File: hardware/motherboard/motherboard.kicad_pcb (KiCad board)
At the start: 2 copper layers, 65 x 56 mm, 5 parts, among them P1 Conn_02x20_Odd_Even

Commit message: imported pcb
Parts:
- moved MK4 235.5 mm to (51.5, 253.1), turned to 270 degrees
- moved MK2 223.9 mm to (100.5, 253.1), turned to 90 degrees
- moved MK3 159.6 mm to (51.5, 195.1), turned to 270 degrees
- moved P1 148.8 mm to (99.2, 200.0), turned to 180 degrees
- moved MK1 141.9 mm to (100.5, 195.1), turned to 90 degrees
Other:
- board size 65 x 56 mm -> 237 x 156.6 mm

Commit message: work on hardware motherboard
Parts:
- removed MK1, MK2, MK3, MK4: M2.5, MountingHole:MountingHole_2.7mm_M2.5
- added C1: 10µF, Capacitor_THT:CP_Radial_D6.3mm_P2.50mm, F.Cu at (266.2, 119.4)
- added C10: 1000µF, Capacitor_THT:CP_Radial_D10.0mm_P5.00mm, F.Cu at (275.8, 123.7)
- added C11: 100nF, Capacitor_THT:C_Disc_D5.0mm_W2.5mm_P5.00mm, F.Cu at (262.8, 170.7)
- added C12: 1000µF, Capacitor_THT:CP_Radial_D10.0mm_P5.00mm, F.Cu at (275.9, 156.5)
- added C13: 1000µF, Capacitor_THT:CP_Radial_D10.0mm_P5.00mm, F.Cu at (275.9, 146.7)
- added C14: 1000µF, Capacitor_THT:CP_Radial_D10.0mm_P5.00mm, F.Cu at (275.7, 184.8)
- added C15: 100nF, Capacitor_THT:C_Disc_D5.0mm_W2.5mm_P5.00mm, F.Cu at (259.7, 127.0)
- added C16: 100nF, Capacitor_THT:C_Disc_D5.0mm_W2.5mm_P5.00mm, F.Cu at (259.2, 165.7)
- added C2: 10µF, Capacitor_THT:CP_Radial_D6.3mm_P2.50mm, F.Cu at (264.3, 157.8)
- added C3: 10µF, Capacitor_THT:CP_Radial_D6.3mm_P2.50mm, F.Cu at (258.1, 119.5)
- added C4: 10µF, Capacitor_THT:CP_Radial_D6.3mm_P2.50mm, F.Cu at (256.1, 157.8)
- added C5: 8n2, Capacitor_THT:C_Disc_D5.0mm_W2.5mm_P5.00mm, F.Cu at (255.8, 131.9)
- added C6: 470µF, Capacitor_THT:CP_Radial_D10.0mm_P5.00mm, F.Cu at (275.9, 135.3)
- added C7: 8n2, Capacitor_THT:C_Disc_D5.0mm_W2.5mm_P5.00mm, F.Cu at (255.2, 170.6)
- added C8: 470µF, Capacitor_THT:CP_Radial_D10.0mm_P5.00mm, F.Cu at (276.1, 167.9)
- added C9: 100nF, Capacitor_THT:C_Disc_D5.0mm_W2.5mm_P5.00mm, F.Cu at (263.4, 131.9)
- added J1: Conn_01x04_Female, Connector_PinSocket_2.54mm:PinSocket_1x04_P2.54mm_Vertical, F.Cu at (161.0, 107.0)
- added J1: Conn_01x04_Female, Connector_PinSocket_2.54mm:PinSocket_1x04_P2.54mm_Vertical, F.Cu at (158.5, 139.3)
- added J10: Conn_01x02_Female, TerminalBlock:TerminalBlock_bornier-2_P5.08mm, F.Cu at (267.0, 194.0)
- added J11: Conn_01x02_Female, TerminalBlock:TerminalBlock_bornier-2_P5.08mm, F.Cu at (255.0, 194.0)
- added J2: AudioJack3_Ground, Connector_Audio:Jack_3.5mm_CUI_SJ-3523-SMT_Horizontal, F.Cu at (270.8, 107.2)
- added J3: Conn_01x05_Female, TerminalBlock:TerminalBlock_bornier-5_P5.08mm, F.Cu at (175.0, 194.4)
- added J4: Conn_01x05_Female, Connector_TE-Connectivity:TE_826576-5_1x05_P3.96mm_Vertical, F.Cu at (195.0, 175.0)
- added J5: Conn_01x05_Female, Connector_PinSocket_2.54mm:PinSocket_1x05_P2.54mm_Vertical, F.Cu at (185.6, 117.0)
- added J6: Conn_01x05_Female, Connector_PinSocket_2.54mm:PinSocket_1x05_P2.54mm_Vertical, F.Cu at (218.0, 117.0)
- added J7: Conn_01x05_Female, Connector_PinSocket_2.54mm:PinSocket_1x05_P2.54mm_Vertical, F.Cu at (219.0, 194.4)
- added J8: Conn_01x02_Female, TerminalBlock:TerminalBlock_bornier-2_P5.08mm, F.Cu at (146.0, 194.4)
- added J9: Conn_01x03_Female, TerminalBlock:TerminalBlock_bornier-3_P5.08mm, F.Cu at (202.0, 194.4)
- added K2: SANYOU_SRD_Form_C, Relay_THT:Relay_SPDT_SANYOU_SRD_Series_Form_C, F.Cu at (174.0, 168.0)
- added Q1: BSS138, Package_TO_SOT_SMD:SOT-23, F.Cu at (171.0, 150.0)
- added Q2: BSS138, Package_TO_SOT_SMD:SOT-23, F.Cu at (160.0, 150.0)
- added Q3: BSS138, Package_TO_SOT_SMD:SOT-23, F.Cu at (147.0, 184.0)
- added R1: 10K, Resistor_THT:R_Axial_DIN0207_L6.3mm_D2.5mm_P7.62mm_Horizontal, F.Cu at (174.6, 154.0)
- added R10: 4R7, Resistor_THT:R_Axial_DIN0207_L6.3mm_D2.5mm_P7.62mm_Horizontal, F.Cu at (263.4, 135.9)
- added R11: 470R, Resistor_THT:R_Axial_DIN0207_L6.3mm_D2.5mm_P7.62mm_Horizontal, F.Cu at (262.9, 184.9)
- added R12: 4R7, Resistor_THT:R_Axial_DIN0207_L6.3mm_D2.5mm_P7.62mm_Horizontal, F.Cu at (262.9, 173.9)
- added R13: 1R, Resistor_THT:R_Axial_DIN0207_L6.3mm_D2.5mm_P7.62mm_Horizontal, F.Cu at (259.7, 143.6)
- added R14: 1R, Resistor_THT:R_Axial_DIN0207_L6.3mm_D2.5mm_P7.62mm_Horizontal, F.Cu at (259.2, 173.9)
- added R15: 10K, Resistor_THT:R_Axial_DIN0207_L6.3mm_D2.5mm_P7.62mm_Horizontal, F.Cu at (167.0, 179.0)
- added R2: 10K, Resistor_THT:R_Axial_DIN0207_L6.3mm_D2.5mm_P7.62mm_Horizontal, F.Cu at (164.0, 154.0)
- added R3: 10K, Resistor_THT:R_Axial_DIN0207_L6.3mm_D2.5mm_P7.62mm_Horizontal, F.Cu at (143.0, 188.0)
- added R4: 10K, Resistor_THT:R_Axial_DIN0207_L6.3mm_D2.5mm_P7.62mm_Horizontal, F.Cu at (167.0, 157.0)
- added R5: 10K, Resistor_THT:R_Axial_DIN0207_L6.3mm_D2.5mm_P7.62mm_Horizontal, F.Cu at (156.4, 157.0)
- added R6: 10K, Resistor_THT:R_Axial_DIN0207_L6.3mm_D2.5mm_P7.62mm_Horizontal, F.Cu at (140.0, 188.0)
- added R7: 100R, Resistor_THT:R_Axial_DIN0207_L6.3mm_D2.5mm_P7.62mm_Horizontal, F.Cu at (255.8, 143.6)
- added R8: 100R, Resistor_THT:R_Axial_DIN0207_L6.3mm_D2.5mm_P7.62mm_Horizontal, F.Cu at (255.2, 181.6)
- added R9: 470R, Resistor_THT:R_Axial_DIN0207_L6.3mm_D2.5mm_P7.62mm_Horizontal, F.Cu at (263.4, 147.6)
- added RV1: 10K, Potentiometer_SMD:Potentiometer_Bourns_3314J_Vertical, F.Cu at (248.3, 119.4)
- added RV2: 10K, Potentiometer_SMD:Potentiometer_Bourns_3314J_Vertical, F.Cu at (248.9, 157.7)
- added U1: TDA2003, Package_TO_SOT_THT:TO-220-5_P3.4x3.7mm_StaggerOdd_Lead3.8mm_Vertical, F.Cu at (246.0, 175.4)
- added U2: TDA2003, Package_TO_SOT_THT:TO-220-5_P3.4x3.7mm_StaggerOdd_Lead3.8mm_Vertical, F.Cu at (246.0, 139.7)
- moved P1 100.4 mm to (56.9, 109.0)
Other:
- board size 237 x 156.6 mm -> 279.3 x 100 mm

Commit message: layout of first mb; test print
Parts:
- removed the J1 at (161.0, 107.0)
- removed the J1 at (158.5, 139.3)
- removed R2, R5: 10K, Resistor_THT:R_Axial_DIN0207_L6.3mm_D2.5mm_P7.62mm_Horizontal
- added C17: 1000µF, Capacitor_THT:CP_Radial_D10.0mm_P5.00mm, F.Cu at (152.5, 127.8)
- added D1: 1N4148W, Diode_SMD:D_SOD-123, F.Cu at (204.8, 184.5)
- added J1: Conn_01x04_Female, Connector_PinSocket_2.54mm:PinSocket_1x04_P2.54mm_Vertical, F.Cu at (139.0, 111.2)
- added J1: Conn_01x04_Female, Connector_PinSocket_2.54mm:PinSocket_1x04_P2.54mm_Vertical, F.Cu at (105.0, 108.7)
- added M1: Fan_3pin, Connector:FanPinHeader_1x03_P2.54mm_Vertical, F.Cu at (103.0, 157.5)
- added M2: Fan_3pin, Connector:FanPinHeader_1x03_P2.54mm_Vertical, F.Cu at (103.0, 148.5)
- J2: value AudioJack3_Ground -> Conn_01x03_Male; footprint Connector_Audio:Jack_3.5mm_CUI_SJ-3523-SMT_Horizontal -> Connector_PinHeader_2.54mm:PinHeader_1x03_P2.54mm_Vertical
- J5: value Conn_01x05_Female -> Conn_01x06_Female; footprint Connector_PinSocket_2.54mm:PinSocket_1x05_P2.54mm_Vertical -> Connector_PinSocket_2.54mm:PinSocket_1x06_P2.54mm_Vertical
- P1: moved to F.Cu
- moved J2 116.7 mm to (154.2, 113.2), turned to 270 degrees
- moved C2 115.7 mm to (159.2, 109.2), turned to 90 degrees
- moved RV2 110.8 mm to (150.2, 107.2), turned to 270 degrees
- moved C1 107.0 mm to (159.2, 117.2), turned to 270 degrees
- moved C4 101.2 mm to (167.2, 109.2), turned to 90 degrees
- moved RV1 98.1 mm to (150.2, 119.2), turned to 270 degrees
- moved C13 97.9 mm to (180.5, 168.5), turned to 0 degrees
- moved C6 97.8 mm to (180.5, 156.8), turned to 0 degrees
- moved C10 97.8 mm to (180.5, 145.5), turned to 0 degrees
- moved J10 91.3 mm to (175.8, 196.0)
- moved U1 91.2 mm to (179.5, 113.0), turned to 0 degrees
- moved C3 90.9 mm to (167.2, 117.2), turned to 270 degrees
- moved C14 79.6 mm to (197.8, 168.5), turned to 0 degrees
- moved R4 79.4 mm to (231.0, 110.0), turned to 180 degrees
- moved C8 79.1 mm to (197.8, 157.0), turned to 0 degrees
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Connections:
- net /MOTOR_SIGNAL renamed Net-(J5-Pad4)
- J3 pad 3: +3V3 -> +12V
- J3 pad 5: +12V -> +3V3
- J5 pad 3: /MOTOR_ZF -> +5V
- J5 pad 5: +5V -> Net-(J5-Pad5)
- J7 pad 2: /M3_HA -> /M1_HA
- J7 pad 4: /M1_HA -> /M3_HA
- K2 pad 2: GND -> Net-(D1-Pad2)
- K2 pad 4: Net-(K2-Pad4) -> GND
- K2 pad 5: /MOTOR_RELAY -> +5V
- P1 pad 1: +3V3 -> Net-(P1-Pad1)
- P1 pad 17: +3V3 -> Net-(P1-Pad1)
- Q2 pad 1: +3V3 -> /GPIO13(PWM1)
- Q2 pad 2: /GPIO13(PWM1) -> GND
- Q2 pad 3: /MOTOR_RELAY -> Net-(D1-Pad2)
- R15 pad 2: /MOTOR_RELAY -> /GPIO13(PWM1)
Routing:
- net +5V: track 0.00 -> 433.2 mm
- net +3V3: track 0.00 -> 232.2 mm
- net /GPIO12(PWM0): track 0.00 -> 199.0 mm, vias 0 -> 1
- net +12V: track 0.00 -> 186.4 mm
- net /GPIO13(PWM1): track 0.00 -> 104.2 mm
- net /GPIO11(SPI0_SCK): track 0.00 -> 98.5 mm
- net /AMP2_LS: track 0.00 -> 93.7 mm
- net /AMP1_LS: track 0.00 -> 90.6 mm
- net /M3_HA: track 0.00 -> 88.4 mm
- net /M2_HA: track 0.00 -> 86.9 mm
- net /M1_HA: track 0.00 -> 85.3 mm
- net /GPIO3(SCL1): track 0.00 -> 73.9 mm
- net /GPIO2(SDA1): track 0.00 -> 73.9 mm
- net Net-(C13-Pad1): track 0.00 -> 71.4 mm
- net Net-(C14-Pad1): track 0.00 -> 71.2 mm
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- added copper zone on B.Cu, net GND
- added copper zone on F.Cu, net GND
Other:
- board size 279.3 x 100 mm -> 160 x 100 mm
- board text removed: "CAMERA"
- board text removed: "DISPLAY"
- board text removed: "RASPBERRY-PI 40-PIN ADDON BOARD VIEW FROM TOP NOTE: P1 SHOULD BE FITTED ON THE REVERSE OF THE BOARD ADD EDGE CUTS FROM CAMERA AND DISPLAY PORTS AS REQUIRED"
- board text removed: "RJ45"
- board text removed: "USB"

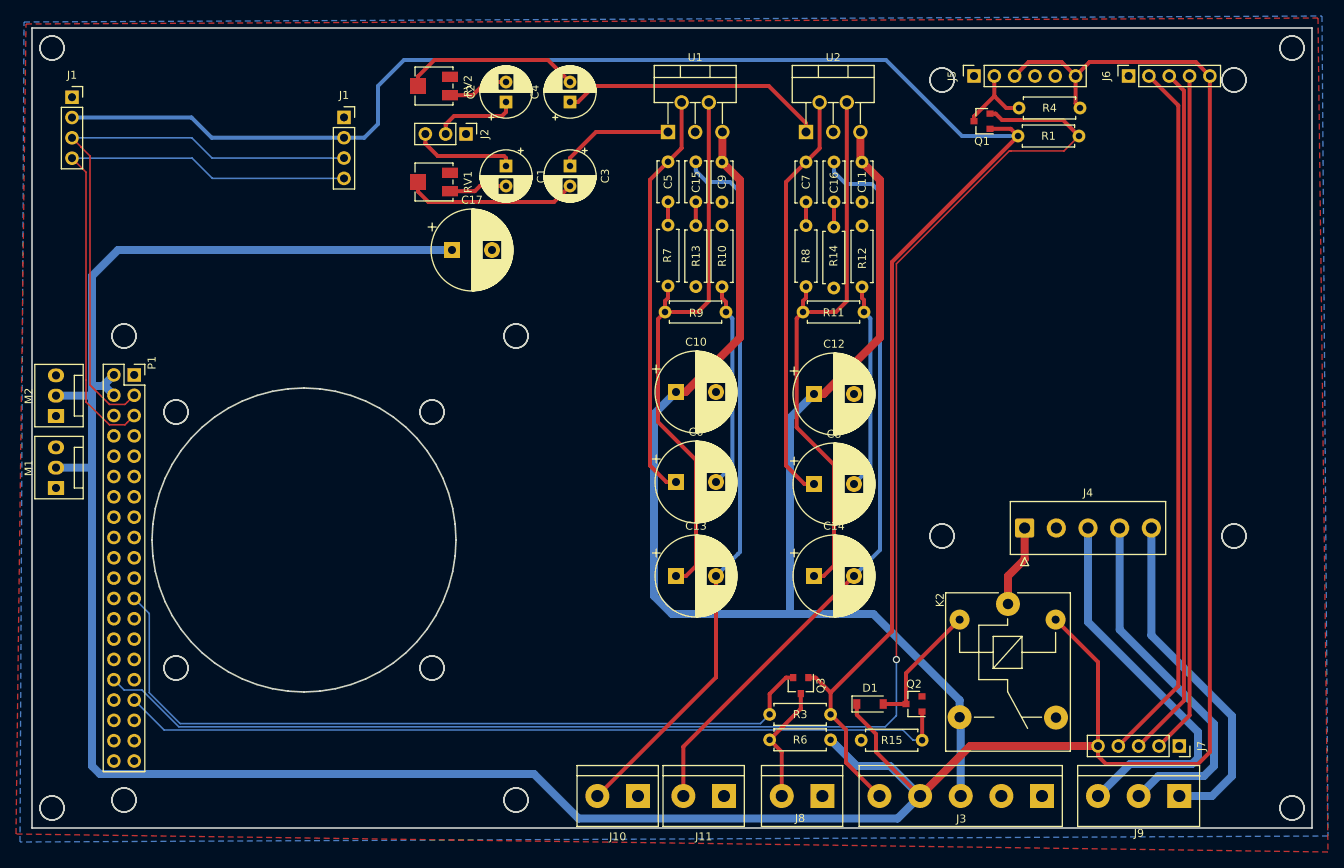
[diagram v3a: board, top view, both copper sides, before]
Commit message: ordered first version
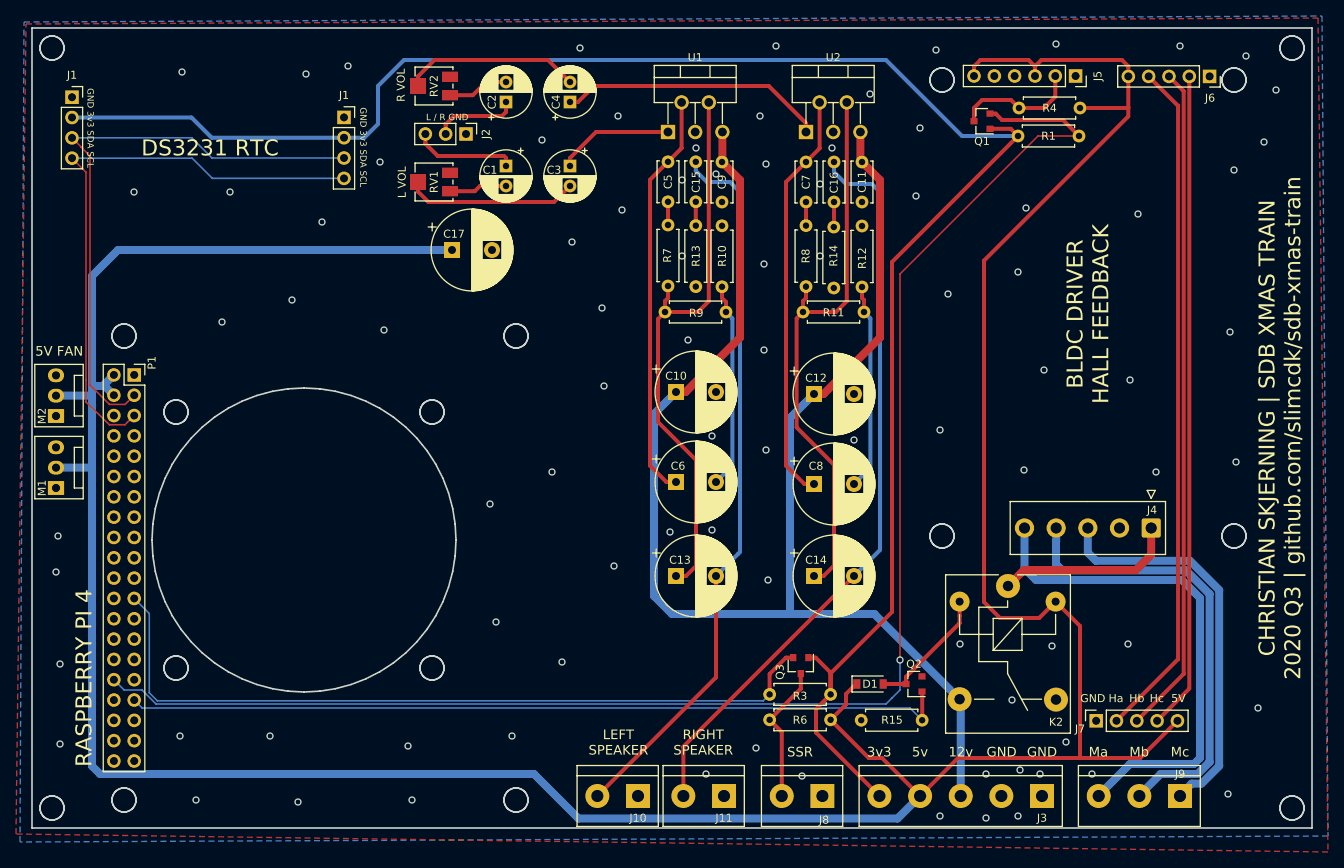
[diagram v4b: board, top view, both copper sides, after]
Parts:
- moved J4 15.8 mm to (239.9, 162.5), turned to 180 degrees
- moved J5 12.7 mm to (230.4, 106.0), turned to 270 degrees
- moved J7 10.9 mm to (233.0, 186.6), turned to 90 degrees
- moved J6 10.1 mm to (247.2, 106.0), turned to 270 degrees
- moved D1 2.50 mm to (204.8, 182.0)
- moved Q2 2.50 mm to (210.2, 182.0)
- moved Q3 2.50 mm to (196.1, 179.7)
- moved R15 2.50 mm to (203.7, 186.5)
- moved R3 2.50 mm to (199.8, 183.3)
- moved R6 2.50 mm to (199.8, 186.5)
- moved K2 2.25 mm to (222.0, 169.8)
- moved J9 0.09 mm to (243.5, 196.0)
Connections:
- J9 pad 1: /M3 -> /M1
- J9 pad 3: /M1 -> /M3
- P1 pad 17: Net-(P1-Pad1) -> Net-(P1-Pad17)
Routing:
- net /M3: track 42.8 -> 63.2 mm
- net Net-(J4-Pad1): track 10.4 -> 22.9 mm
- net +5V: track 433.2 -> 421.2 mm
- net /M2: track 45.6 -> 56.9 mm
- net /M3_HA: track 88.4 -> 82.2 mm
- net /MOTOR_VR: track 10.4 -> 15.8 mm
- net /GPIO12(PWM0): track 199.0 -> 194.0 mm
- net +3V3: track 232.2 -> 236.4 mm
- net /M2_HA: track 86.9 -> 83.7 mm
- net /SSR_RELAY: track 15.0 -> 17.5 mm
- net /GPIO11(SPI0_SCK): track 98.5 -> 97.2 mm
- net /M1: track 48.9 -> 50.0 mm
- net /GPIO13(PWM1): track 104.2 -> 103.1 mm
- net (no net): vias 0 -> 90
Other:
- board text added: "12v"
- board text added: "3v3"
- board text added: "5V"
- board text added: "5V FAN"
- board text added: "5v"
- board text added: "BLDC DRIVER HALL FEEDBACK"
- board text added: "CHRISTIAN SKJERNING | SDB XMAS TRAIN 2020 Q3 | github.com/slimcdk/sdb-xmas-train"
- board text added: "DS3231 RTC"
- board text added: "GND"
- board text added: "GND 3v3 SDA SCL"
- board text added: "Ha"
- board text added: "Hb"
- board text added: "Hc"
- board text added: "L / R GND"
- board text added: "L VOL"
- board text added: "LEFT SPEAKER"
- board text added: "Ma"
- board text added: "Mb"
- board text added: "Mc"
- board text added: "R VOL"
- board text added: "RASPBERRY PI 4"
- board text added: "RIGHT SPEAKER"
- board text added: "SSR"

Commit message: pcb design v2
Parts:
- removed the J1 at (105.0, 108.7)
- removed M1, M2: Fan_3pin, Connector:FanPinHeader_1x03_P2.54mm_Vertical
- added C18: 1000µF, Capacitor_THT:CP_Radial_D5.0mm_P2.50mm, F.Cu at (28.5, 56.2)
- added D2: LED, LED_SMD:LED_1210_3225Metric_Pad1.42x2.65mm_HandSolder, F.Cu at (105.8, 122.8)
- added D3: LED, LED_SMD:LED_1210_3225Metric_Pad1.42x2.65mm_HandSolder, F.Cu at (105.8, 130.2)
- added D4: LED, LED_SMD:LED_1210_3225Metric_Pad1.42x2.65mm_HandSolder, F.Cu at (105.8, 137.8)
- added D5: LED, LED_SMD:LED_1210_3225Metric_Pad1.42x2.65mm_HandSolder, F.Cu at (28.5, 78.0)
- added D6: LED, LED_SMD:LED_1210_3225Metric_Pad1.42x2.65mm_HandSolder, F.Cu at (185.8, 73.6)
- added D7: LED, LED_SMD:LED_1210_3225Metric_Pad1.42x2.65mm_HandSolder, F.Cu at (173.6, 58.4)
- added D8: LED, LED_SMD:LED_1210_3225Metric_Pad1.42x2.65mm_HandSolder, F.Cu at (163.5, 38.5)
- added D9: LED, LED_SMD:LED_1210_3225Metric_Pad1.42x2.65mm_HandSolder, F.Cu at (104.5, 63.0)
- added J12: Conn_01x03_Male, Connector:FanPinHeader_1x03_P2.54mm_Vertical, F.Cu at (103.6, 147.7)
- added J13: Conn_01x03_Male, Connector:FanPinHeader_1x03_P2.54mm_Vertical, F.Cu at (113.3, 147.7)
- added J14: Conn_01x03_Male, Connector:FanPinHeader_1x03_P2.54mm_Vertical, F.Cu at (123.0, 147.7)
- added J15: Conn_01x06_Female, Connector_PinSocket_2.54mm:PinSocket_1x06_P2.54mm_Vertical, F.Cu at (58.0, 29.6)
- added R16: 10K, Resistor_SMD:R_1210_3225Metric_Pad1.42x2.65mm_HandSolder, B.Cu at (51.0, 106.8)
- added R17: ?, Resistor_SMD:R_1210_3225Metric_Pad1.42x2.65mm_HandSolder, F.Cu at (185.8, 79.0)
- added R18: ?, Resistor_SMD:R_1210_3225Metric_Pad1.42x2.65mm_HandSolder, F.Cu at (173.6, 64.3)
- added R19: 10K, Resistor_SMD:R_1210_3225Metric_Pad1.42x2.65mm_HandSolder, B.Cu at (47.0, 106.8)
- added R2: ?, Resistor_SMD:R_1210_3225Metric_Pad1.42x2.65mm_HandSolder, F.Cu at (105.8, 126.6)
- added R20: ?, Resistor_SMD:R_1210_3225Metric_Pad1.42x2.65mm_HandSolder, F.Cu at (167.5, 38.5)
- added R21: ?, Resistor_SMD:R_1210_3225Metric_Pad1.42x2.65mm_HandSolder, F.Cu at (104.4, 57.5)
- added R5: ?, Resistor_SMD:R_1210_3225Metric_Pad1.42x2.65mm_HandSolder, F.Cu at (28.5, 74.5)
- added REF**: Unknown_TO220_16x24mm_Heatsink, Local_Heatsink:Unknown_TO220_16x24mm_Heatsink, F.Cu at (172.2, 142.4)
- added REF**: Unknown_TO220_16x24mm_Heatsink, Local_Heatsink:Unknown_TO220_16x24mm_Heatsink, F.Cu at (143.7, 142.3)
- added TR1: TRANSF5, Local_Transformer_Audio:MURATA_DA10XJ_Audo_Transformer, F.Cu at (124.7, 88.4)
- added TR2: TRANSF5, Local_Transformer_Audio:MURATA_DA10XJ_Audo_Transformer, F.Cu at (108.5, 88.4)
- C17: footprint Capacitor_THT:CP_Radial_D10.0mm_P5.00mm -> Capacitor_THT:CP_Radial_D5.0mm_P2.50mm
- D1: footprint Diode_SMD:D_SOD-123 -> Diode_SMD:D_SOD-128
- Q1, Q2, Q3: footprint Package_TO_SOT_SMD:SOT-23 -> Package_TO_SOT_SMD:SOT-23_Handsoldering; moved to B.Cu
- R1, R4: value 10K -> ?; footprint Resistor_THT:R_Axial_DIN0207_L6.3mm_D2.5mm_P7.62mm_Horizontal -> Resistor_SMD:R_1210_3225Metric_Pad1.42x2.65mm_HandSolder
- R10, R11, R12, R13, R14, R7, R8, R9: footprint Resistor_THT:R_Axial_DIN0207_L6.3mm_D2.5mm_P7.62mm_Horizontal -> Resistor_SMD:R_1210_3225Metric_Pad1.42x2.65mm_HandSolder
- R15, R3, R6: footprint Resistor_THT:R_Axial_DIN0207_L6.3mm_D2.5mm_P7.62mm_Horizontal -> Resistor_SMD:R_1210_3225Metric_Pad1.42x2.65mm_HandSolder; moved to B.Cu
- moved Q2 173.4 mm to (57.6, 99.8), turned to 90 degrees
- moved Q1 170.1 mm to (49.0, 99.8), turned to 90 degrees
- moved R15 168.1 mm to (55.6, 106.8), turned to 90 degrees
- moved R3 155.7 mm to (64.2, 106.8), turned to 270 degrees
- moved D1 155.0 mm to (180.0, 29.0), turned to 180 degrees
- moved J6 154.6 mm to (109.0, 36.8), turned to 0 degrees
- moved R6 153.9 mm to (68.2, 106.8), turned to 270 degrees
- moved Q3 152.5 mm to (66.2, 99.8), turned to 90 degrees
- moved J9 148.7 mm to (194.5, 55.6), turned to 270 degrees
- moved J3 144.5 mm to (92.8, 140.5), turned to 90 degrees
- moved K2 142.7 mm to (180.0, 33.4)
- moved J4 139.9 mm to (165.4, 44.0), turned to 270 degrees
- moved C17 139.8 mm to (28.5, 63.2), turned to 270 degrees
- moved J5 132.4 mm to (109.0, 53.5), turned to 0 degrees
- moved J7 129.1 mm to (185.1, 66.8), turned to 180 degrees
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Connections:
- net /AMP1_LS renamed Net-(C13-Pad2)
- net /AMP2_LS renamed Net-(C14-Pad2)
- C1 pad 1: /AMP1_IN -> Net-(C1-Pad1)
- C2 pad 1: /AMP2_IN -> Net-(C2-Pad1)
- J2 pad 1: GND -> Net-(J2-Pad1)
- J2 pad 2: /AMP2_IN -> Net-(J2-Pad2)
- J2 pad 3: /AMP1_IN -> Net-(J2-Pad3)
- J5 pad 2: /MOTOR_VR -> Net-(J5-Pad2)
- J8 pad 2: /SSR_RELAY -> Net-(J8-Pad2)
- Q1 pad 3: /MOTOR_VR -> Net-(J5-Pad2)
- Q3 pad 3: /SSR_RELAY -> Net-(J8-Pad2)
- R1 pad 1: +3V3 -> Net-(D2-Pad2)
- R1 pad 2: /GPIO12(PWM0) -> +3V3
- R3 pad 1: +3V3 -> /GPIO11(SPI0_SCK)
- R3 pad 2: /GPIO11(SPI0_SCK) -> GND
- R4 pad 1: +5V -> Net-(D4-Pad2)
- R4 pad 2: /MOTOR_VR -> +12V
- R6 pad 1: +5V -> Net-(J8-Pad2)
- R6 pad 2: /SSR_RELAY -> +5V
- RV1 pad 3: GND -> Net-(RV1-Pad3)
- RV2 pad 3: GND -> Net-(RV2-Pad3)
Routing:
- net Net-(D1-Pad2): track 15.9 -> 189.2 mm, vias 0 -> 1
- net /GPIO12(PWM0): track 194.0 -> 32.5 mm
- net Net-(J8-Pad2): track 0.00 -> 158.5 mm, vias 0 -> 1
- net Net-(J5-Pad2): track 0.00 -> 111.8 mm
- net /GPIO13(PWM1): track 103.1 -> 187.3 mm, vias 0 -> 3
- net Net-(C3-Pad1): track 14.6 -> 85.6 mm, vias 0 -> 1
- net +3V3: track 236.4 -> 179.7 mm, vias 0 -> 2
- net /GPIO11(SPI0_SCK): track 97.2 -> 51.5 mm, vias 0 -> 1
- net Net-(J2-Pad1): track 0.00 -> 43.1 mm, vias 0 -> 1
- net Net-(C13-Pad2): track 90.6 -> 50.5 mm
- net /M3_HA: track 82.2 -> 121.5 mm
- net Net-(J2-Pad2): track 0.00 -> 35.6 mm
- net /M2_HA: track 83.7 -> 117.9 mm
- net /M1_HA: track 85.3 -> 114.5 mm
- net +12V: track 186.4 -> 158.9 mm, vias 0 -> 23
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- added copper zone on B.Cu, net +12V
- added copper zone on F.Cu, net +12V
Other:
- board size 160 x 100 mm -> 175 x 127 mm
- board text added: "12V FAN"
- board text added: "12V RAIL"
- board text added: "BLDC DRIVER W/ HALL FEEDBACK"
- board text added: "CHRISTIAN SKJERNING SDB XMAS TRAIN v2 2020 Q3 www.github.com/slimcdk/sdb- xmas-train.git"
- board text added: "GPIO11"
- board text added: "RASPBERRY PI"
- board text added: "TIP RING SLEEVE"
- board text removed: "BLDC DRIVER HALL FEEDBACK"
- board text removed: "CHRISTIAN SKJERNING | SDB XMAS TRAIN 2020 Q3 | github.com/slimcdk/sdb-xmas-train"
- board text removed: "L / R GND"
- board text removed: "L VOL"
- board text removed: "R VOL"
- board text removed: "RASPBERRY PI 4"
- board text removed: "SSR"
